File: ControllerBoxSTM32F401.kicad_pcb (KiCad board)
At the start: 2 copper layers, 20 parts, among them U1 YAAJ_WeAct_BlackPill_Part_Lik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

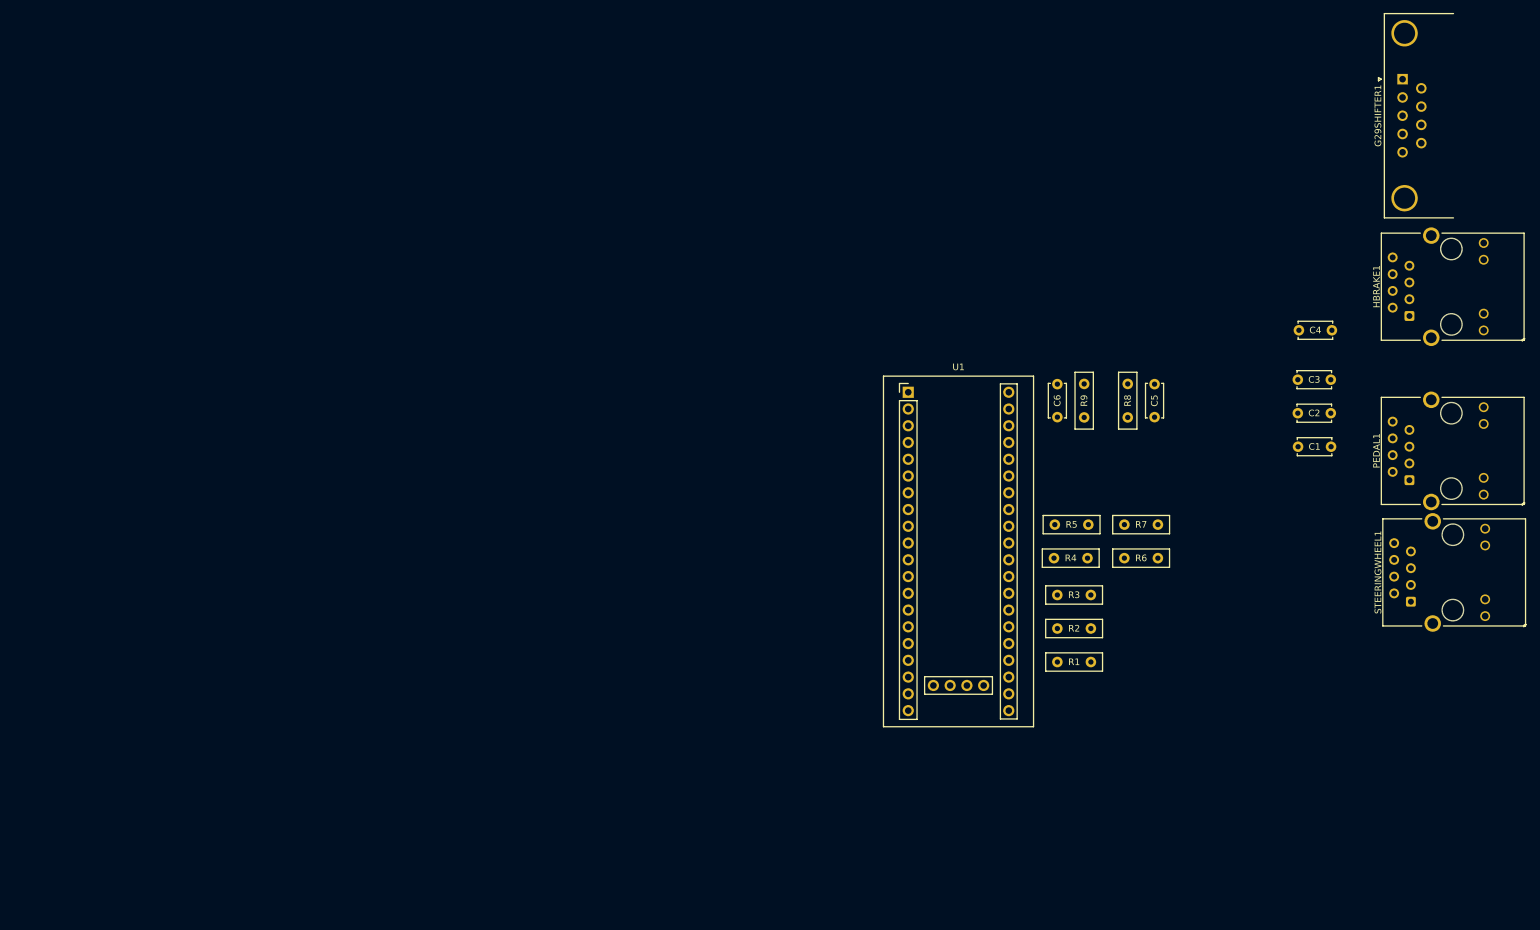
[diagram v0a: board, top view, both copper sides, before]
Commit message: update PCB and create edge cuts
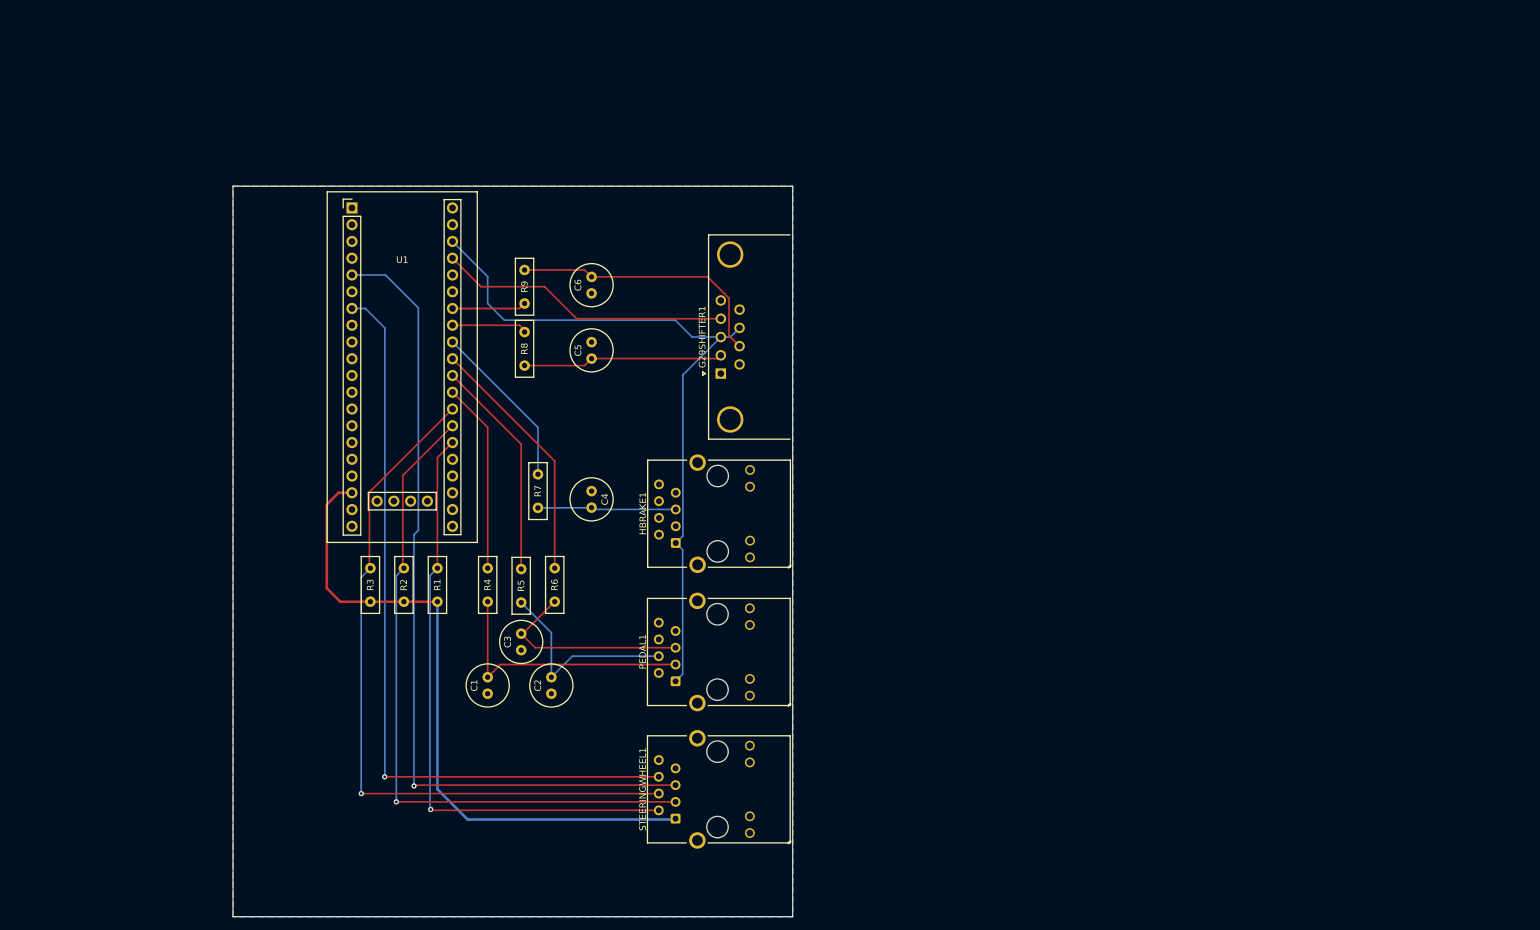
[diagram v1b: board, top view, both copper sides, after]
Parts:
- C1, C2, C3, C4, C5, C6: footprint Capacitor_THT:C_Disc_D5.0mm_W2.5mm_P5.00mm -> Capacitor_THT:C_Radial_D6.3mm_H7.0mm_P2.50mm
- G29SHIFTER1: value DB9_Female -> DB9_Male; footprint Connector_Dsub:DSUB-9_Female_Horizontal_P2.77x2.84mm_EdgePinOffset4.94mm_Housed_MountingHolesOffset7.48mm -> Connector_Dsub:DSUB-9_Male_Horizontal_P2.77x2.84mm_EdgePinOffset7.70mm_Housed_MountingHolesOffset9.12mm
- moved C1 132.5 mm to (110.2, 128.3), turned to -90 degrees
- moved C3 124.7 mm to (115.3, 124.2), turned to 90 degrees
- moved C2 120.9 mm to (119.9, 130.8), turned to 90 degrees
- moved HBRAKE1 116.4 mm to (138.7, 107.9)
- moved STEERINGWHEEL1 116.2 mm to (138.7, 149.7)
- moved PEDAL1 115.4 mm to (138.7, 128.9)
- moved G29SHIFTER1 112.6 mm to (145.6, 82.3)
- moved C4 110.0 mm to (126.0, 100.1), turned to -90 degrees
- moved R3 109.2 mm to (92.5, 116.8), turned to 90 degrees
- moved R2 104.2 mm to (97.5, 116.8), turned to 90 degrees
- moved R1 99.5 mm to (102.6, 116.8), turned to 90 degrees
- moved R7 94.0 mm to (117.9, 102.6), turned to 90 degrees
- moved R6 91.7 mm to (120.4, 116.8), turned to 90 degrees
- moved R8 91.5 mm to (115.8, 81.0), turned to 90 degrees
- moved R4 91.2 mm to (110.2, 116.8), turned to 90 degrees
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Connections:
- U1 pad 18: unconnected-(U1-Pad18) -> VCC 5V
- U1 pad 19: unconnected-(U1-Pad19) -> GND
- U1 pad 20: unconnected-(U1-Pad20) -> VCC 3.3V
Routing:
- net PWM: track 0.00 -> 125.0 mm, vias 0 -> 1
- net DIR: track 0.00 -> 115.8 mm, vias 0 -> 1
- net ENC Z: track 0.00 -> 109.3 mm, vias 0 -> 1
- net VCC 3.3V: track 0.00 -> 108.4 mm
- net ENC B: track 0.00 -> 103.0 mm, vias 0 -> 1
- net VCC 5V: track 0.00 -> 101.4 mm
- net ENC A: track 0.00 -> 91.7 mm, vias 0 -> 1
- net REVERSE: track 0.00 -> 44.5 mm
- net ACCEL: track 0.00 -> 40.7 mm
- net SHIFTER Y: track 0.00 -> 40.7 mm
- net Net-(R6-Pad2): track 0.00 -> 38.2 mm
- net Net-(R5-Pad2): track 0.00 -> 33.7 mm
- net CLUTCH: track 0.00 -> 31.4 mm
- net BRAKE: track 0.00 -> 30.9 mm
- net SHIFTER X: track 0.00 -> 30.4 mm
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- added copper zone on B.Cu, net GND
- added copper zone on F.Cu, net GND
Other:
- board outline added: 84.8 x 110.7 mm

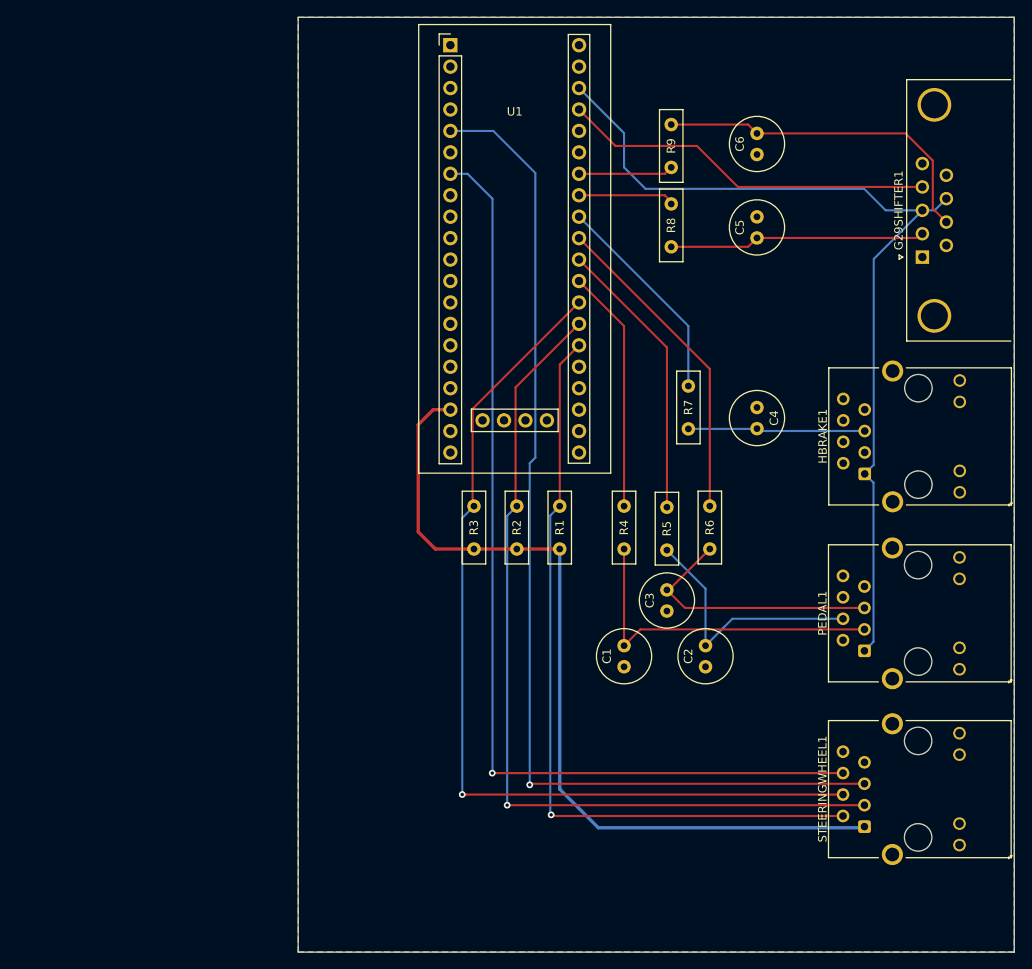
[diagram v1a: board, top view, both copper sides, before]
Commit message: add button matrix to PCB
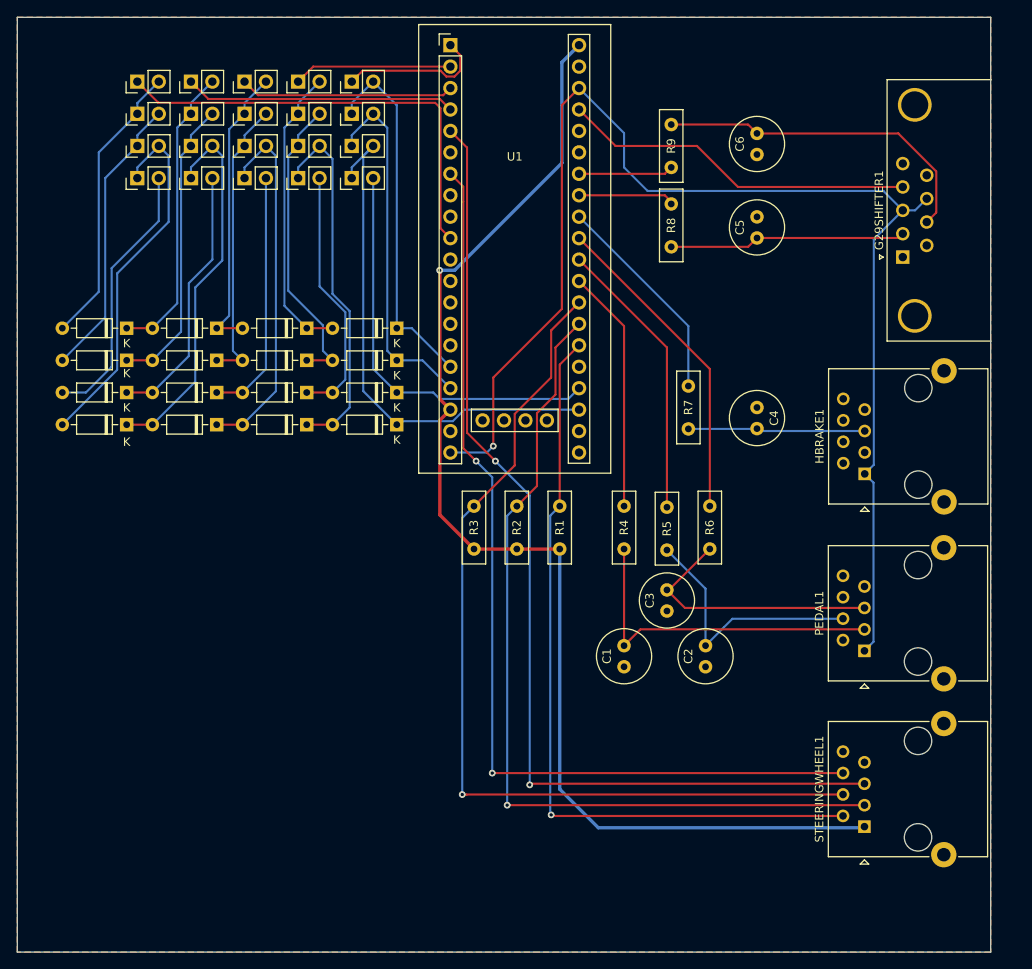
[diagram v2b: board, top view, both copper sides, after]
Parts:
- added D1: 1N4148, Diode_THT:D_DO-35_SOD27_P7.62mm_Horizontal, F.Cu at (83.3, 90.7)
- added D10: 1N4148, Diode_THT:D_DO-35_SOD27_P7.62mm_Horizontal, F.Cu at (72.6, 102.1)
- added D11: 1N4148, Diode_THT:D_DO-35_SOD27_P7.62mm_Horizontal, F.Cu at (62.0, 102.1)
- added D12: 1N4148, Diode_THT:D_DO-35_SOD27_P7.62mm_Horizontal, F.Cu at (51.3, 102.1)
- added D13: 1N4148, Diode_THT:D_DO-35_SOD27_P7.62mm_Horizontal, F.Cu at (83.3, 98.3)
- added D14: 1N4148, Diode_THT:D_DO-35_SOD27_P7.62mm_Horizontal, F.Cu at (72.6, 98.3)
- added D15: 1N4148, Diode_THT:D_DO-35_SOD27_P7.62mm_Horizontal, F.Cu at (62.0, 98.3)
- added D16: 1N4148, Diode_THT:D_DO-35_SOD27_P7.62mm_Horizontal, F.Cu at (51.3, 98.3)
- added D2: 1N4148, Diode_THT:D_DO-35_SOD27_P7.62mm_Horizontal, F.Cu at (72.6, 90.7)
- added D3: 1N4148, Diode_THT:D_DO-35_SOD27_P7.62mm_Horizontal, F.Cu at (62.0, 90.7)
- added D4: 1N4148, Diode_THT:D_DO-35_SOD27_P7.62mm_Horizontal, F.Cu at (51.3, 90.7)
- added D5: 1N4148, Diode_THT:D_DO-35_SOD27_P7.62mm_Horizontal, F.Cu at (83.3, 94.5)
- added D6: 1N4148, Diode_THT:D_DO-35_SOD27_P7.62mm_Horizontal, F.Cu at (72.6, 94.5)
- added D7: 1N4148, Diode_THT:D_DO-35_SOD27_P7.62mm_Horizontal, F.Cu at (62.0, 94.5)
- added D8: 1N4148, Diode_THT:D_DO-35_SOD27_P7.62mm_Horizontal, F.Cu at (51.3, 94.5)
- added D9: 1N4148, Diode_THT:D_DO-35_SOD27_P7.62mm_Horizontal, F.Cu at (83.3, 102.1)
- added SW1: Switch, Connector_PinHeader_2.54mm:PinHeader_1x02_P2.54mm_Vertical, F.Cu at (78.0, 61.5)
- added SW10: Switch, Connector_PinHeader_2.54mm:PinHeader_1x02_P2.54mm_Vertical, F.Cu at (52.6, 65.3)
- added SW11: Switch, Connector_PinHeader_2.54mm:PinHeader_1x02_P2.54mm_Vertical, F.Cu at (78.0, 69.1)
- added SW12: Switch, Connector_PinHeader_2.54mm:PinHeader_1x02_P2.54mm_Vertical, F.Cu at (71.6, 69.1)
- added SW13: Switch, Connector_PinHeader_2.54mm:PinHeader_1x02_P2.54mm_Vertical, F.Cu at (65.3, 69.1)
- added SW14: Switch, Connector_PinHeader_2.54mm:PinHeader_1x02_P2.54mm_Vertical, F.Cu at (58.9, 69.1)
- added SW15: Switch, Connector_PinHeader_2.54mm:PinHeader_1x02_P2.54mm_Vertical, F.Cu at (52.6, 69.1)
- added SW16: Switch, Connector_PinHeader_2.54mm:PinHeader_1x02_P2.54mm_Vertical, F.Cu at (78.0, 72.9)
- added SW17: Switch, Connector_PinHeader_2.54mm:PinHeader_1x02_P2.54mm_Vertical, F.Cu at (71.6, 72.9)
- added SW18: Switch, Connector_PinHeader_2.54mm:PinHeader_1x02_P2.54mm_Vertical, F.Cu at (65.3, 72.9)
- added SW19: Switch, Connector_PinHeader_2.54mm:PinHeader_1x02_P2.54mm_Vertical, F.Cu at (58.9, 72.9)
- added SW2: Switch, Connector_PinHeader_2.54mm:PinHeader_1x02_P2.54mm_Vertical, F.Cu at (71.6, 61.5)
- added SW20: Switch, Connector_PinHeader_2.54mm:PinHeader_1x02_P2.54mm_Vertical, F.Cu at (52.6, 72.9)
- added SW3: Switch, Connector_PinHeader_2.54mm:PinHeader_1x02_P2.54mm_Vertical, F.Cu at (65.3, 61.5)
- added SW4: Switch, Connector_PinHeader_2.54mm:PinHeader_1x02_P2.54mm_Vertical, F.Cu at (58.9, 61.5)
- added SW5: Switch, Connector_PinHeader_2.54mm:PinHeader_1x02_P2.54mm_Vertical, F.Cu at (52.6, 61.5)
- added SW6: Switch, Connector_PinHeader_2.54mm:PinHeader_1x02_P2.54mm_Vertical, F.Cu at (78.0, 65.3)
- added SW7: Switch, Connector_PinHeader_2.54mm:PinHeader_1x02_P2.54mm_Vertical, F.Cu at (71.6, 65.3)
- added SW8: Switch, Connector_PinHeader_2.54mm:PinHeader_1x02_P2.54mm_Vertical, F.Cu at (65.3, 65.3)
- added SW9: Switch, Connector_PinHeader_2.54mm:PinHeader_1x02_P2.54mm_Vertical, F.Cu at (58.9, 65.3)
- HBRAKE1, PEDAL1, STEERINGWHEEL1: footprint Connector_RJ:RJ45_Hanrun_HR911105A -> Connector_RJ:RJ45_Ninigi_GE
- moved G29SHIFTER1 2.32 mm to (143.3, 82.3)
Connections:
- G29SHIFTER1 pad 0: (no net) -> GND
- HBRAKE1 pad SH: (no net) -> GND
- PEDAL1 pad SH: (no net) -> GND
- STEERINGWHEEL1 pad SH: (no net) -> GND
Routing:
- net BTN_COL3: track 0.00 -> 62.3 mm
- net BTN_ROW5: track 0.00 -> 53.1 mm
- net BTN_COL4: track 0.00 -> 49.0 mm
- net VCC 3.3V: track 108.4 -> 157.1 mm, vias 0 -> 1
- net VCC 5V: track 101.4 -> 146.9 mm, vias 0 -> 1
- net Net-(SW14-Pad2): track 0.00 -> 44.8 mm
- net Net-(SW15-Pad2): track 0.00 -> 43.6 mm
- net BTN_COL1: track 0.00 -> 43.5 mm
- net Net-(SW12-Pad2): track 0.00 -> 43.2 mm
- net Net-(SW13-Pad2): track 0.00 -> 43.1 mm
- net BTN_COL2: track 0.00 -> 42.9 mm
- net Net-(SW12-Pad1): track 0.00 -> 36.0 mm
- net Net-(SW14-Pad1): track 0.00 -> 35.2 mm
- net Net-(SW4-Pad2): track 0.00 -> 35.2 mm
- net Net-(SW2-Pad2): track 0.00 -> 35.1 mm
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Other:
- board size 84.8 x 110.7 mm -> 115.3 x 110.7 mm
